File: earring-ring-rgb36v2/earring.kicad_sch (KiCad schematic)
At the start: 59 parts, among them J1 Conn_01x05, Q1 AO3401A, Q2 Q_Photo_NPN_EC, SW1 SW_Push, U2 STM32L031G6Ux, Y1 Crystal

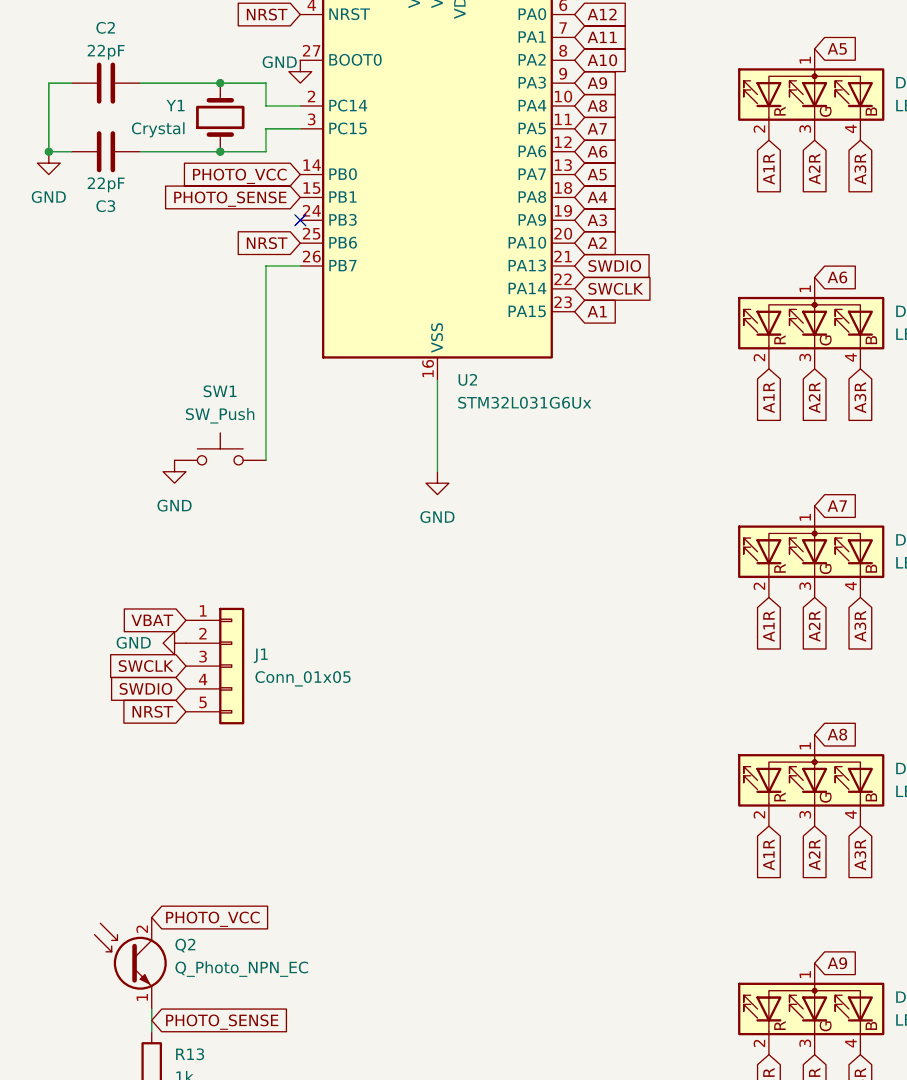
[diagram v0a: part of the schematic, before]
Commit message: earring-ring-rgb36v2: add microphone
This also required reworking the PCB a little.
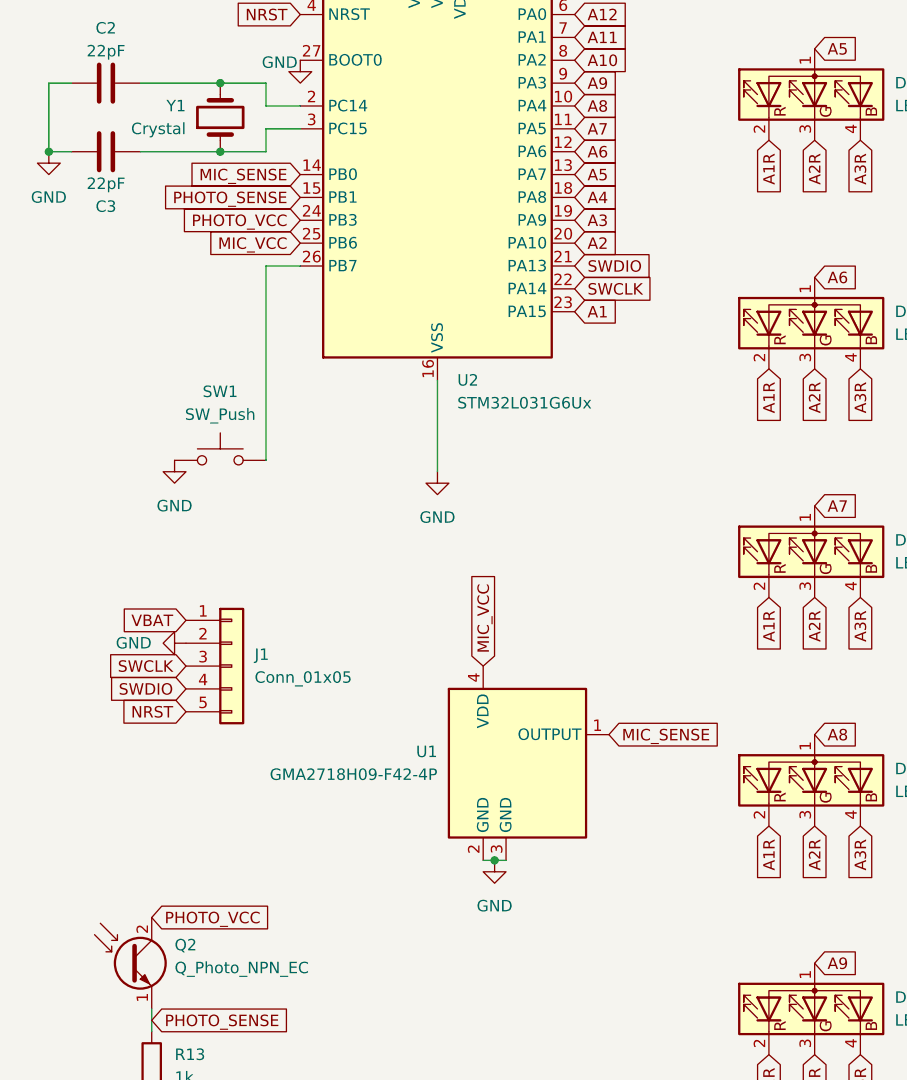
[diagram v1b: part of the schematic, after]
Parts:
- added U1: GMA2718H09-F42-4P, Custom:GMA2718H09-F42-4P, symbol Custom:GMA2718H09-F42-4P
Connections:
- net GND: now also U1.2 (GND), U1.3 (GND)
- net NRST: no longer U2.25 (PB6)
- net PHOTO_VCC: now also U2.24 (PB3); no longer U2.14 (PB0)
- new net MIC_SENSE: U1.1 (OUTPUT), U2.14 (PB0)
- new net MIC_VCC: U1.4 (VDD), U2.25 (PB6)
- no-connect marks 1 -> 0
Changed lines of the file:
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@@
 	)
 	(junction
+		(at 69.85 133.35)
+		(diameter 0)
+		(color 0 0 0 0)
+	)
+	(junction
 		(at 66.04 22.86)
 		(diameter 0)
@@
 		(color 0 0 0 0)
 	)
-	(no_connect
-		(at 48.26 62.23)
-	)
 	(wire
 		(pts
@@
 	(wire
 		(pts
+			(xy 68.58 133.35) (xy 69.85 133.35)
+		)
+		(stroke
+			(width 0)
+			(type default)
+		)
+	)
+	(wire
+		(pts
 			(xy 44.45 67.31) (xy 44.45 88.9)
 		)
@@
 	(wire
 		(pts
+			(xy 69.85 133.35) (xy 71.12 133.35)
+		)
+		(stroke
+			(width 0)
+			(type default)
+		)
+	)
+	(wire
+		(pts
 			(xy 44.45 67.31) (xy 48.26 67.31)
 		)
@@
 		)
 	)
-	(global_label "NRST"
-		(shape input)
-		(at 48.26 64.77 180)
-		(fields_autoplaced yes)
-		(effects
-			(font
-				(size 1.27 1.27)
-			)
-			(justify right)
-		)
-		(property "Intersheetrefs" "${INTERSHEET_REFS}"
-			(at 40.4972 64.77 0)
-			(effects
-				(font
-					(size 1.27 1.27)
-				)
-				(justify right)
-				(hide yes)
-			)
-		)
-	)
 	(global_label "A1R"
 		(shape input)
@@
 		)
 	)
+	(global_label "MIC_SENSE"
+		(shape input)
+		(at 48.26 57.15 180)
+		(fields_autoplaced yes)
+		(effects
+			(font
+				(size 1.27 1.27)
+			)
+			(justify right)
+		)
+		(property "Intersheetrefs" "${INTERSHEET_REFS}"
+			(at 34.9335 57.15 0)
+			(effects
+				(font
+					(size 1.27 1.27)
+				)
+				(justify right)
+				(hide yes)
+			)
+		)
+	)
 	(global_label "A4"
 		(shape input)
@@
 		)
 	)
+	(global_label "PHOTO_VCC"
+		(shape input)
+		(at 48.26 62.23 180)
+		(fields_autoplaced yes)
+		(effects
+			(font
+				(size 1.27 1.27)
+			)
+			(justify right)
+		)
+		(property "Intersheetrefs" "${INTERSHEET_REFS}"
+			(at 34.4495 62.23 0)
+			(effects
+				(font
+					(size 1.27 1.27)
+				)
+				(justify right)
+				(hide yes)
+			)
+		)
+	)
 	(global_label "A3R"
 		(shape input)
@@
 		)
 	)
+	(global_label "MIC_SENSE"
+		(shape input)
+		(at 82.55 119.38 0)
+		(fields_autoplaced yes)
+		(effects
+			(font
+				(size 1.27 1.27)
+			)
+			(justify left)
+		)
+		(property "Intersheetrefs" "${INTERSHEET_REFS}"
+			(at 95.8765 119.38 0)
+			(effects
+				(font
+					(size 1.27 1.27)
+				)
+				(justify left)
+				(hide yes)
+			)
+		)
+	)
 	(global_label "A5"
 		(shape input)
@@
 		)
 	)
-	(global_label "PHOTO_VCC"
-		(shape input)
-		(at 48.26 57.15 180)
-		(fields_autoplaced yes)
-		(effects
-			(font
-				(size 1.27 1.27)
-			)
-			(justify right)
-		)
-		(property "Intersheetrefs" "${INTERSHEET_REFS}"
-			(at 34.4495 57.15 0)
-			(effects
-				(font
-					(size 1.27 1.27)
-				)
-				(justify right)
-				(hide yes)
-			)
-		)
-	)
 	(global_label "A2"
 		(shape input)
@@
 		)
 	)
+	(global_label "MIC_VCC"
+		(shape input)
+		(at 48.26 64.77 180)
+		(fields_autoplaced yes)
+		(effects
+			(font
+				(size 1.27 1.27)
+			)
+			(justify right)
+		)
+		(property "Intersheetrefs" "${INTERSHEET_REFS}"
+			(at 37.3524 64.77 0)
+			(effects
+				(font
+					(size 1.27 1.27)
+				)
+				(justify right)
+				(hide yes)
+			)
+		)
+	)
 	(global_label "A7R"
 		(shape input)
@@
 		)
 	)
+	(global_label "MIC_VCC"
+		(shape input)
+		(at 68.58 111.76 90)
+		(fields_autoplaced yes)
+		(effects
+			(font
+				(size 1.27 1.27)
+			)
+			(justify left)
+		)
+		(property "Intersheetrefs" "${INTERSHEET_REFS}"
+			(at 68.58 100.8524 90)
+			(effects
+				(font
+					(size 1.27 1.27)
+				)
+				(justify left)
+				(hide yes)
+			)
+		)
+	)
 	(global_label "A9"
 		(shape input)
@@
 	)
 	(symbol
+		(lib_id "power:GND")
+		(at 69.85 133.35 0)
+		(unit 1)
+		(exclude_from_sim no)
+		(in_bom yes)
+		(on_board yes)
+		(dnp no)
+		(fields_autoplaced yes)
+		(property "Reference" "#PWR06"
+			(at 69.85 139.7 0)
+			(effects
+				(font
+					(size 1.27 1.27)
+				)
+				(hide yes)
+			)
+		)
+		(property "Value" "GND"
+			(at 69.85 138.43 0)
+			(effects
+				(font
+					(size 1.27 1.27)
+				)
+			)
+		)
+		(property "Footprint" ""
+			(at 69.85 133.35 0)
+			(effects
+				(font
+					(size 1.27 1.27)
+				)
+				(hide yes)
+			)
+		)
+		(property "Datasheet" ""
+			(at 69.85 133.35 0)
+			(effects
+				(font
+					(size 1.27 1.27)
+				)
+				(hide yes)
+			)
+		)
+		(property "Description" "Power symbol creates a global label with name \"GND\" , ground"
+			(at 69.85 133.35 0)
+			(effects
+				(font
+					(size 1.27 1.27)
+				)
+				(hide yes)
+			)
+		)
+		(pin "1"
+		)
+		(instances
+			(project "earring"
+				(path "/5b672b97-2486-4be1-9927-7141d9b63fb2"
+					(reference "#PWR06")
+					(unit 1)
+				)
+			)
+		)
+	)
+	(symbol
 		(lib_id "Device:LED_ARGB")
 		(at 168.91 48.26 90)
@@
 					(unit 1)
 				)
+			)
+		)
+	)
+	(symbol
+		(lib_id "Custom:GMA2718H09-F42-4P")
+		(at 72.39 121.92 0)
+		(unit 1)
+		(exclude_from_sim no)
+		(in_bom yes)
+		(on_board yes)
+		(dnp no)
+		(fields_autoplaced yes)
+		(property "Reference" "U1"
+			(at 63.5 121.2849 0)
+			(effects
+				(font
+					(size 1.27 1.27)
+				)
+				(justify right)
+			)
+		)
+		(property "Value" "GMA2718H09-F42-4P"
+			(at 63.5 123.8249 0)
+			(effects
+				(font
+					(size 1.27 1.27)
+				)
+				(justify right)
+			)
+		)
+		(property "Footprint" "Custom:GMA2718H09-F42-4P"
+			(at 72.39 121.92 0)
+			(effects
+				(font
+					(size 1.27 1.27)
+				)
+				(hide yes)
+			)
+		)
+		(property "Datasheet" ""
+			(at 72.39 121.92 0)
+			(effects
+				(font
+					(size 1.27 1.27)
+				)
+				(hide yes)
+			)
+		)
+		(property "Description" ""
+			(at 72.39 121.92 0)
+			(effects
+				(font
+					(size 1.27 1.27)
+				)
+				(hide yes)
+			)
+		)
+		(pin "4"
+		)
+		(pin "1"
+		)
+		(pin "3"
+		)
+		(pin "2"
+		)
+		(instances
+			(project ""
+				(path "/5b672b97-2486-4be1-9927-7141d9b63fb2"
+					(reference "U1")
+					(unit 1)
+				)

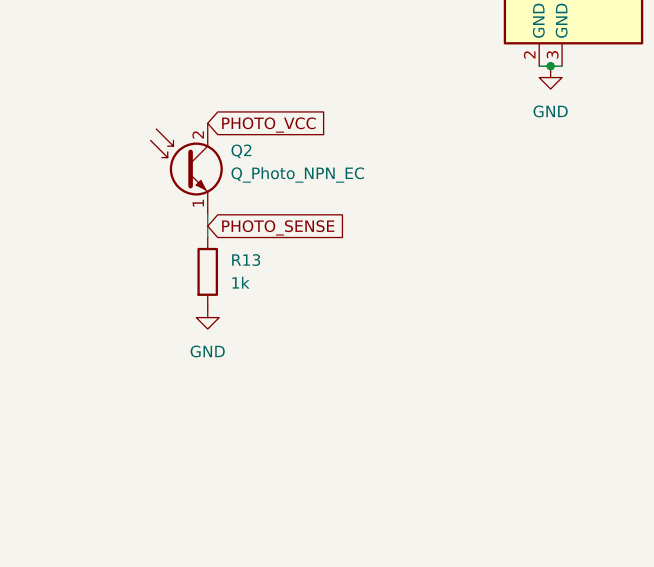
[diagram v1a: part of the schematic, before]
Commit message: earring-ring-rgb36v2: switch to 10k resistor for light sensing
Based on some very rough measurements and calculations, I think this
will end up as ~2V input voltage on the ADC on a bright 400 nits
display.

This is also the version that was sent to JLCPCB as a test production.
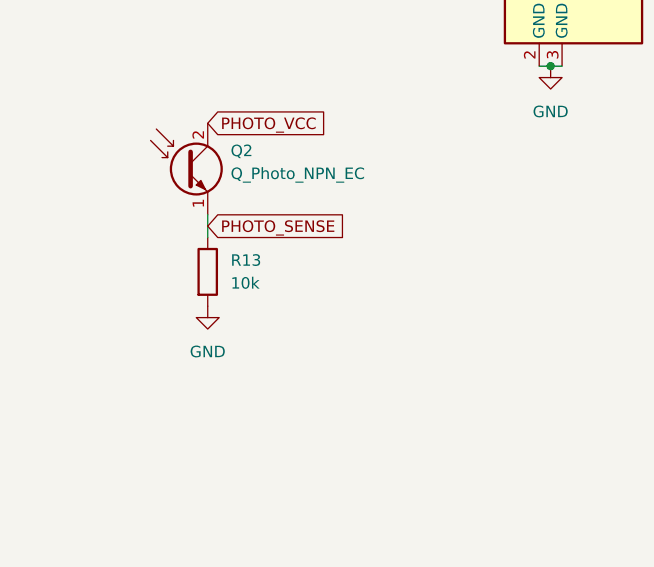
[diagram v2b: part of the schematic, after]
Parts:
- R13: value 1k -> 10k; LCSC C11702 -> C25756
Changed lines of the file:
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@@
 			)
 		)
-		(property "Value" "1k"
+		(property "Value" "10k"
 			(at 34.29 157.4799 0)
 			(effects
@@
 			)
 		)
-		(property "LCSC" "C11702"
+		(property "LCSC" "C25756"
 			(at 31.75 156.21 0)
 			(effects

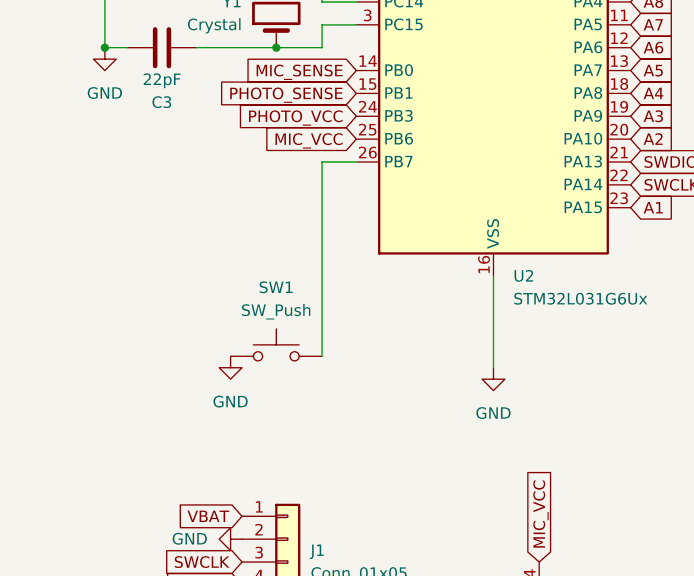
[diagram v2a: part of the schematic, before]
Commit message: earring-ring-rgb36v2: add extra button for program/color selection
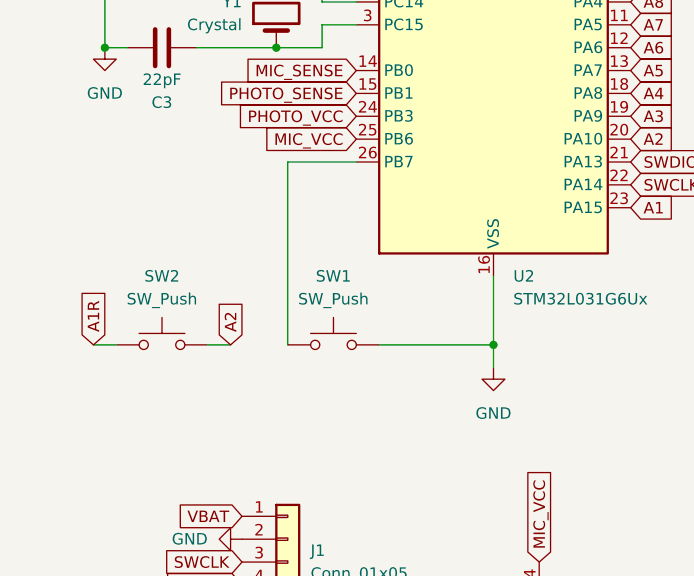
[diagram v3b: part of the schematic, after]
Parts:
- added SW2: SW_Push, Custom:KXT311LHS, symbol Switch:SW_Push
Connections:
- net A1R: now also SW2.1
- net A2: now also SW2.2
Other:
- moved on the sheet: SW1
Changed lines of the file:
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@@
 	)
 	(junction
+		(at 63.5 87.63)
+		(diameter 0)
+		(color 0 0 0 0)
+	)
+	(junction
 		(at 69.85 133.35)
 		(diameter 0)
@@
 	(wire
 		(pts
+			(xy 40.64 67.31) (xy 48.26 67.31)
+		)
+		(stroke
+			(width 0)
+			(type default)
+		)
+	)
+	(wire
+		(pts
+			(xy 63.5 87.63) (xy 63.5 90.17)
+		)
+		(stroke
+			(width 0)
+			(type default)
+		)
+	)
+	(wire
+		(pts
 			(xy 31.75 152.4) (xy 31.75 149.86)
 		)
@@
 	(wire
 		(pts
-			(xy 44.45 67.31) (xy 44.45 88.9)
+			(xy 34.29 87.63) (xy 31.75 87.63)
 		)
 		(stroke
@@
 	(wire
 		(pts
-			(xy 63.5 80.01) (xy 63.5 90.17)
+			(xy 50.8 87.63) (xy 63.5 87.63)
+		)
+		(stroke
+			(width 0)
+			(type default)
+		)
+	)
+	(wire
+		(pts
+			(xy 63.5 80.01) (xy 63.5 87.63)
 		)
 		(stroke
@@
 	(wire
 		(pts
-			(xy 57.15 22.86) (xy 60.96 22.86)
+			(xy 40.64 67.31) (xy 40.64 87.63)
 		)
 		(stroke
@@
 	(wire
 		(pts
-			(xy 60.96 22.86) (xy 60.96 31.75)
+			(xy 57.15 22.86) (xy 60.96 22.86)
 		)
 		(stroke
@@
 	(wire
 		(pts
-			(xy 29.21 30.48) (xy 39.37 30.48)
+			(xy 60.96 22.86) (xy 60.96 31.75)
 		)
 		(stroke
@@
 	(wire
 		(pts
-			(xy 69.85 133.35) (xy 71.12 133.35)
+			(xy 29.21 30.48) (xy 39.37 30.48)
 		)
 		(stroke
@@
 	(wire
 		(pts
-			(xy 44.45 67.31) (xy 48.26 67.31)
+			(xy 69.85 133.35) (xy 71.12 133.35)
 		)
 		(stroke
@@
 		)
 	)
+	(wire
+		(pts
+			(xy 19.05 87.63) (xy 21.59 87.63)
+		)
+		(stroke
+			(width 0)
+			(type default)
+		)
+	)
 	(global_label "A6R"
 		(shape input)
@@
 		)
 	)
+	(global_label "A2"
+		(shape input)
+		(at 34.29 87.63 90)
+		(fields_autoplaced yes)
+		(effects
+			(font
+				(size 1.27 1.27)
+			)
+			(justify left)
+		)
+		(property "Intersheetrefs" "${INTERSHEET_REFS}"
+			(at 34.29 82.3467 90)
+			(effects
+				(font
+					(size 1.27 1.27)
+				)
+				(justify left)
+				(hide yes)
+			)
+		)
+	)
 	(global_label "A12R"
 		(shape input)
@@
 		)
 	)
+	(global_label "A1R"
+		(shape input)
+		(at 19.05 87.63 90)
+		(fields_autoplaced yes)
+		(effects
+			(font
+				(size 1.27 1.27)
+			)
+			(justify left)
+		)
+		(property "Intersheetrefs" "${INTERSHEET_REFS}"
+			(at 19.05 81.0767 90)
+			(effects
+				(font
+					(size 1.27 1.27)
+				)
+				(justify left)
+				(hide yes)
+			)
+		)
+	)
 	(global_label "A12R"
 		(shape input)
@@
 	)
 	(symbol
+		(lib_id "Switch:SW_Push")
+		(at 26.67 87.63 0)
+		(unit 1)
+		(exclude_from_sim no)
+		(in_bom yes)
+		(on_board yes)
+		(dnp no)
+		(fields_autoplaced yes)
+		(property "Reference" "SW2"
+			(at 26.67 80.01 0)
+			(effects
+				(font
+					(size 1.27 1.27)
+				)
+			)
+		)
+		(property "Value" "SW_Push"
+			(at 26.67 82.55 0)
+			(effects
+				(font
+					(size 1.27 1.27)
+				)
+			)
+		)
+		(property "Footprint" "Custom:KXT311LHS"
+			(at 26.67 82.55 0)
+			(effects
+				(font
+					(size 1.27 1.27)
+				)
+				(hide yes)
+			)
+		)
+		(property "Datasheet" "~"
+			(at 26.67 82.55 0)
+			(effects
+				(font
+					(size 1.27 1.27)
+				)
+				(hide yes)
+			)
+		)
+		(property "Description" "Push button switch, generic, two pins"
+			(at 26.67 87.63 0)
+			(effects
+				(font
+					(size 1.27 1.27)
+				)
+				(hide yes)
+			)
+		)
+		(pin "1"
+		)
+		(pin "2"
+		)
+		(instances
+			(project "earring"
+				(path "/5b672b97-2486-4be1-9927-7141d9b63fb2"
+					(reference "SW2")
+					(unit 1)
+				)
+			)
+		)
+	)
+	(symbol
 		(lib_id "Device:R")
 		(at 245.11 50.8 90)
@@
 	)
 	(symbol
-		(lib_id "power:GND")
-		(at 34.29 88.9 0)
-		(unit 1)
-		(exclude_from_sim no)
-		(in_bom yes)
-		(on_board yes)
-		(dnp no)
-		(fields_autoplaced yes)
-		(property "Reference" "#PWR01"
-			(at 34.29 95.25 0)
-			(effects
-				(font
-					(size 1.27 1.27)
-				)
-				(hide yes)
-			)
-		)
-		(property "Value" "GND"
-			(at 34.29 93.98 0)
-			(effects
-				(font
-					(size 1.27 1.27)
-				)
-			)
-		)
-		(property "Footprint" ""
-			(at 34.29 88.9 0)
-			(effects
-				(font
-					(size 1.27 1.27)
-				)
-				(hide yes)
-			)
-		)
-		(property "Datasheet" ""
-			(at 34.29 88.9 0)
-			(effects
-				(font
-					(size 1.27 1.27)
-				)
-				(hide yes)
-			)
-		)
-		(property "Description" "Power symbol creates a global label with name \"GND\" , ground"
-			(at 34.29 88.9 0)
-			(effects
-				(font
-					(size 1.27 1.27)
-				)
-				(hide yes)
-			)
-		)
-		(pin "1"
-		)
-		(instances
-			(project "earring"
-				(path "/5b672b97-2486-4be1-9927-7141d9b63fb2"
-					(reference "#PWR01")
-					(unit 1)
-				)
-			)
-		)
-	)
-	(symbol
 		(lib_id "Device:LED_ARGB")
 		(at 137.16 200.66 90)
@@
 	(symbol
 		(lib_id "Switch:SW_Push")
-		(at 39.37 88.9 0)
+		(at 45.72 87.63 0)
+		(mirror y)
 		(unit 1)
 		(exclude_from_sim no)
@@
 		(on_board yes)
 		(dnp no)
-		(fields_autoplaced yes)
 		(property "Reference" "SW1"
-			(at 39.37 81.28 0)
+			(at 45.72 80.01 0)
 			(effects
 				(font
@@
 		)
 		(property "Value" "SW_Push"
-			(at 39.37 83.82 0)
+			(at 45.72 82.55 0)
 			(effects
 				(font
@@
 		)
 		(property "Footprint" "Button_Switch_SMD:SW_Push_SPST_NO_Alps_SKRK"
-			(at 39.37 83.82 0)
+			(at 45.72 82.55 0)
 			(effects
 				(font
@@
 		)
 		(property "Datasheet" "~"
-			(at 39.37 83.82 0)
+			(at 45.72 82.55 0)
 			(effects
 				(font
@@
 		)
 		(property "Description" "Push button switch, generic, two pins"
-			(at 39.37 88.9 0)
+			(at 45.72 87.63 0)
 			(effects
 				(font
@@
 		)
 		(property "LCSC" "C561519"
-			(at 39.37 88.9 0)
+			(at 45.72 87.63 0)
 			(effects
 				(font
